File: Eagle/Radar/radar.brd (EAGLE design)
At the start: 100 x 80 mm, 72 parts, among them IC4 MAX414ESD, X1 STEREOJACK, X2 BU-SMA-G, X3 BU-SMA-G, X4 BU-SMA-G

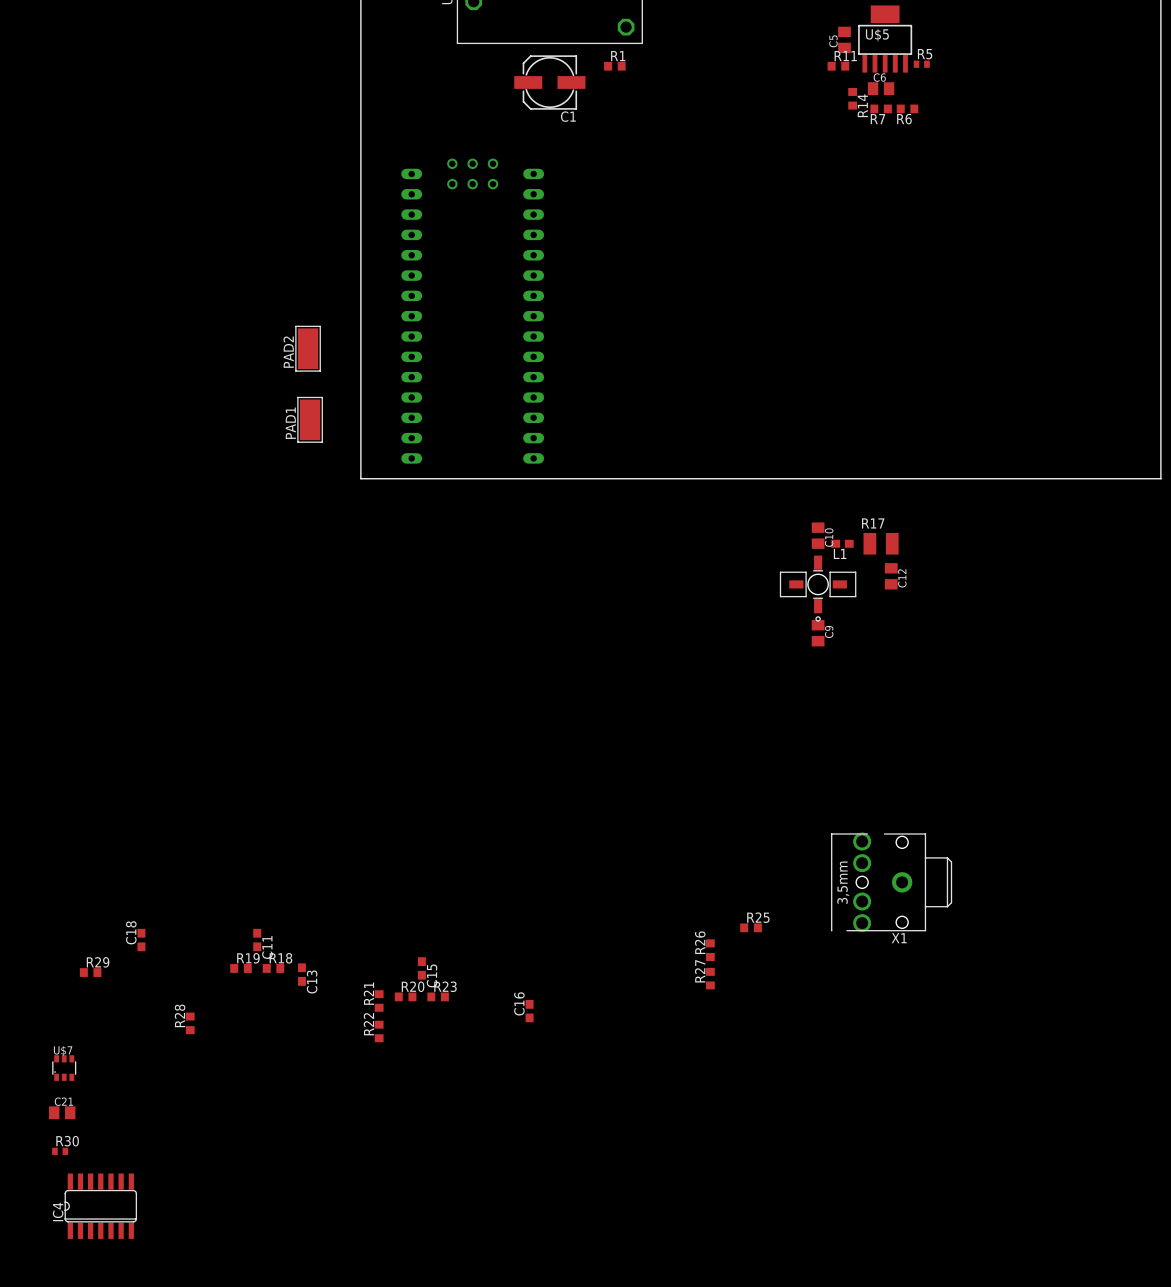
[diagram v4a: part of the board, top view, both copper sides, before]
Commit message: Moved some board parts
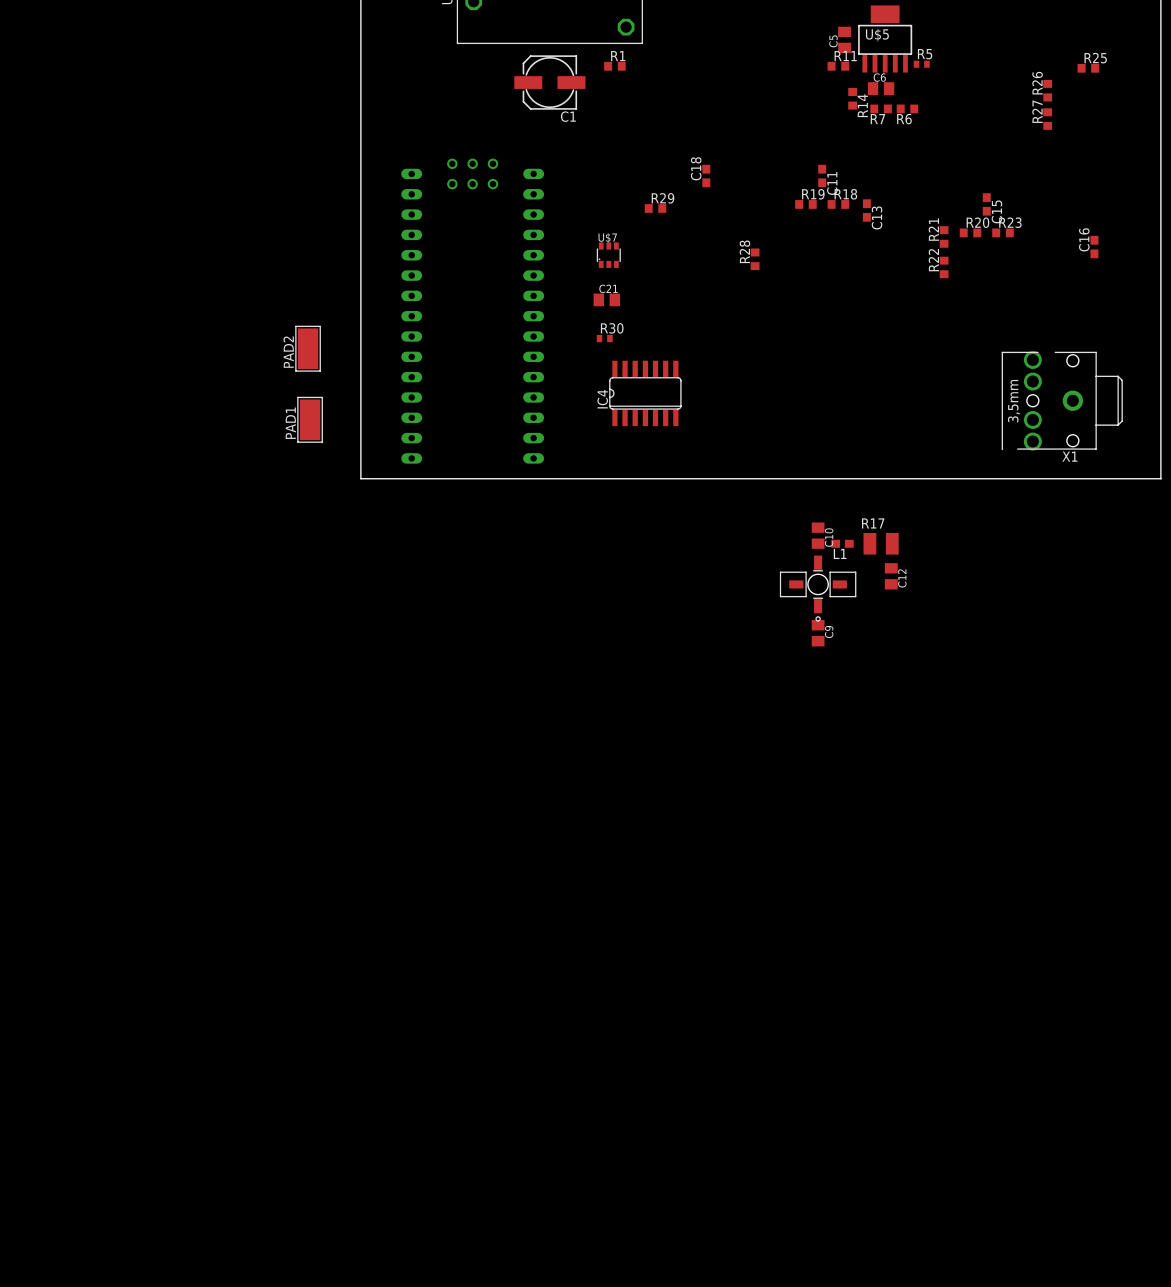
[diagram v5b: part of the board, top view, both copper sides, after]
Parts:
- moved C21 122.3 mm to (30.7, 22.4)
- moved IC4 122.3 mm to (35.6, 10.7)
- moved R30 122.3 mm to (30.5, 17.5)
- moved U$7 122.3 mm to (31.0, 27.9)
- moved C16 118.8 mm to (91.7, 29.0)
- moved R20 118.8 mm to (76.2, 30.7)
- moved R21 118.8 mm to (72.9, 30.2)
- moved R28 118.8 mm to (49.3, 27.4)
- moved C11 118.8 mm to (57.7, 37.8)
- moved C13 118.8 mm to (63.2, 33.5)
- moved C15 118.8 mm to (78.2, 34.3)
- moved C18 118.8 mm to (43.2, 37.8)
- moved R18 118.8 mm to (59.7, 34.3)
- moved R19 118.8 mm to (55.6, 34.3)
- moved R22 118.8 mm to (72.9, 26.4)
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
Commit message: Nearly completed placements on board
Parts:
- removed R11, R12, R13, R14, R25: 0, rcl:R0603
- removed R30, R5: 0, rcl:R0402
- added C24, C25, C8: 10uF, rcl:C0805K
- added L4: 56 nH, radar:0603
- added SJ1, SJ2, SJ3, SJ4, SJ5, SJ6, SJ7, SJ8, SJ9: (no value), jumper:SJ
- added U$11: ERA3+, radar:ERA3+
- R2: value 0 -> 191, 1/2W; device rcl:R0402 -> rcl:R1210
- moved JP3 329.0 mm to (38.4, 74.7)
- moved JP2 321.2 mm to (26.7, 75.7)
- moved JP1 272.4 mm to (32.8, 67.3), turned to 270 degrees
- moved C7 272.3 mm to (82.8, 11.9)
- moved U$10 262.9 mm to (32.8, 62.0)
- moved R32 258.3 mm to (81.8, 18.5)
- moved U$9 256.1 mm to (7.87, 17.0)
- moved R24 255.0 mm to (67.3, 26.7), turned to 270 degrees
- moved L3 252.0 mm to (46.2, 11.2), turned to 270 degrees
- moved U$6 251.0 mm to (39.6, 16.5)
- moved C20 247.9 mm to (81.8, 2.03)
- moved R8 246.1 mm to (73.7, 4.32), turned to 90 degrees
- moved C22 220.1 mm to (60.7, 14.7), turned to 270 degrees
- moved C23 219.1 mm to (50.5, 13.5), turned to 90 degrees
- moved L2 217.4 mm to (27.4, 6.60), turned to 270 degrees
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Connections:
- net N$2 renamed ATTEN_OUT
- net PLL_OUT renamed PLL_IN
- new net LNA_IN: C8.1, U$11.1
- new net LNA_OUT: C24.2, L4.2, U$11.3
- new net LNA_VCC: L4.1, R2.1
- new net MOTOR_GATE: SJ9.2, U$10.1
- new net N$3: C8.2, X3.1
- net AUD1_AC: now also SJ2.2; no longer R25.2
- net GND: now also C25.2, U$11.2, U$11.4
- net LDO1_EN: now also SJ5.2; no longer R2.2
- net LDO1_IN: now also SJ5.1, SJ6.2; no longer R12.2, R2.1
- net LDO1_OUT: now also SJ4.1; no longer R13.1
- net LDO2_EN: now also SJ8.2; no longer R5.2
- net LDO2_IN: now also SJ7.2, SJ8.1; no longer R11.2, R5.1
- net LDO2_OUT: now also SJ3.1; no longer R14.1
- net LFA2_+: now also IC4.12; no longer IC4.5
- net LFA2_-: now also IC4.13; no longer IC4.6
- net LFA2_OUT: now also IC4.14; no longer IC4.7
- net LFA3_OUT: now also SJ2.1; no longer R25.1
- net MAX268X_SHDN: now also SJ1.1; no longer R30.1
- net MOTOR_CTRL: now also SJ9.1; no longer U$10.1
- net PP10V: now also C25.1, R2.2, SJ4.2, SJ7.1; no longer R11.1, R13.2
- net PP10V4: now also SJ6.1; no longer R12.1
- net PP5V: now also SJ1.2, SJ3.2; no longer R14.2, R30.2
- net RF_RX: now also C24.1; no longer X3.1
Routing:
- net LFA1_OUT: track 0.00 -> 2.67 mm
- net LFA2_+: track 0.00 -> 1.86 mm

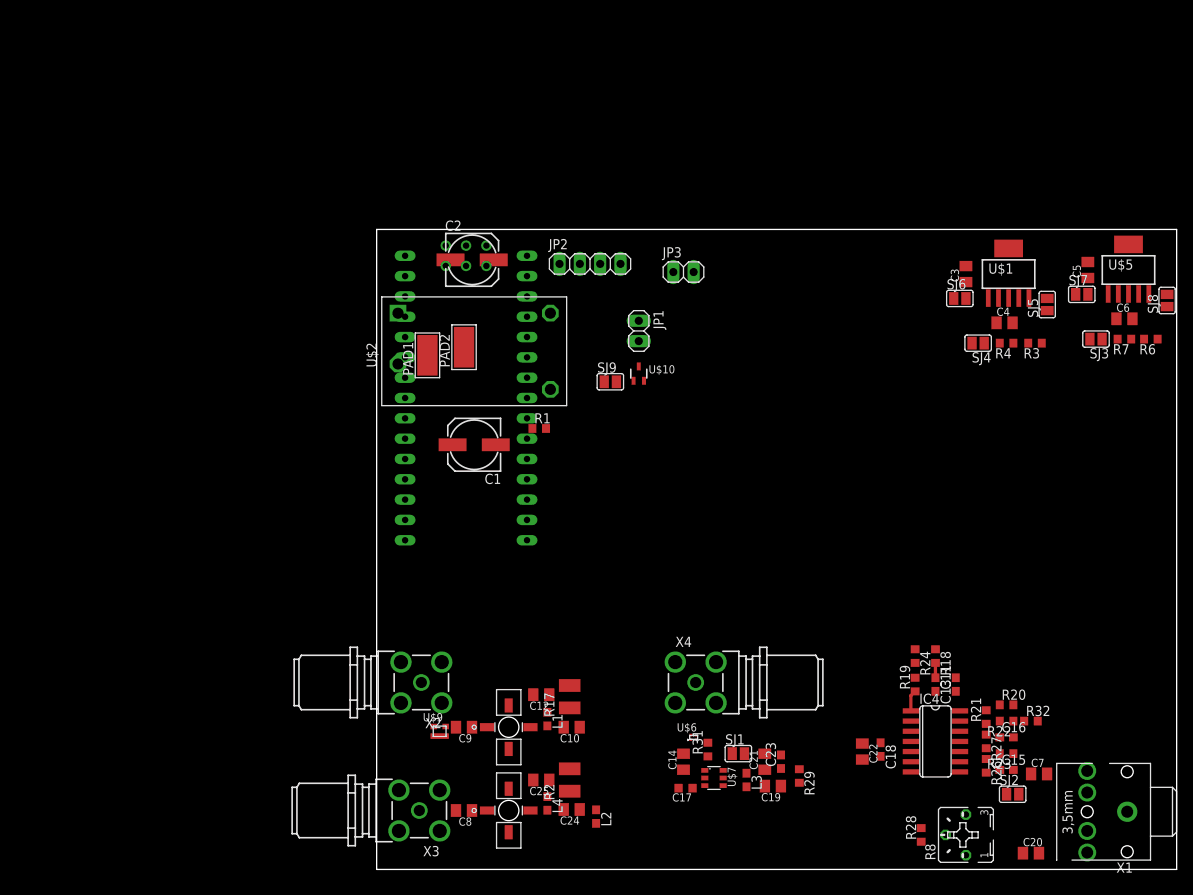
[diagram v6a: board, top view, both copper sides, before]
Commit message: Finished RF routing
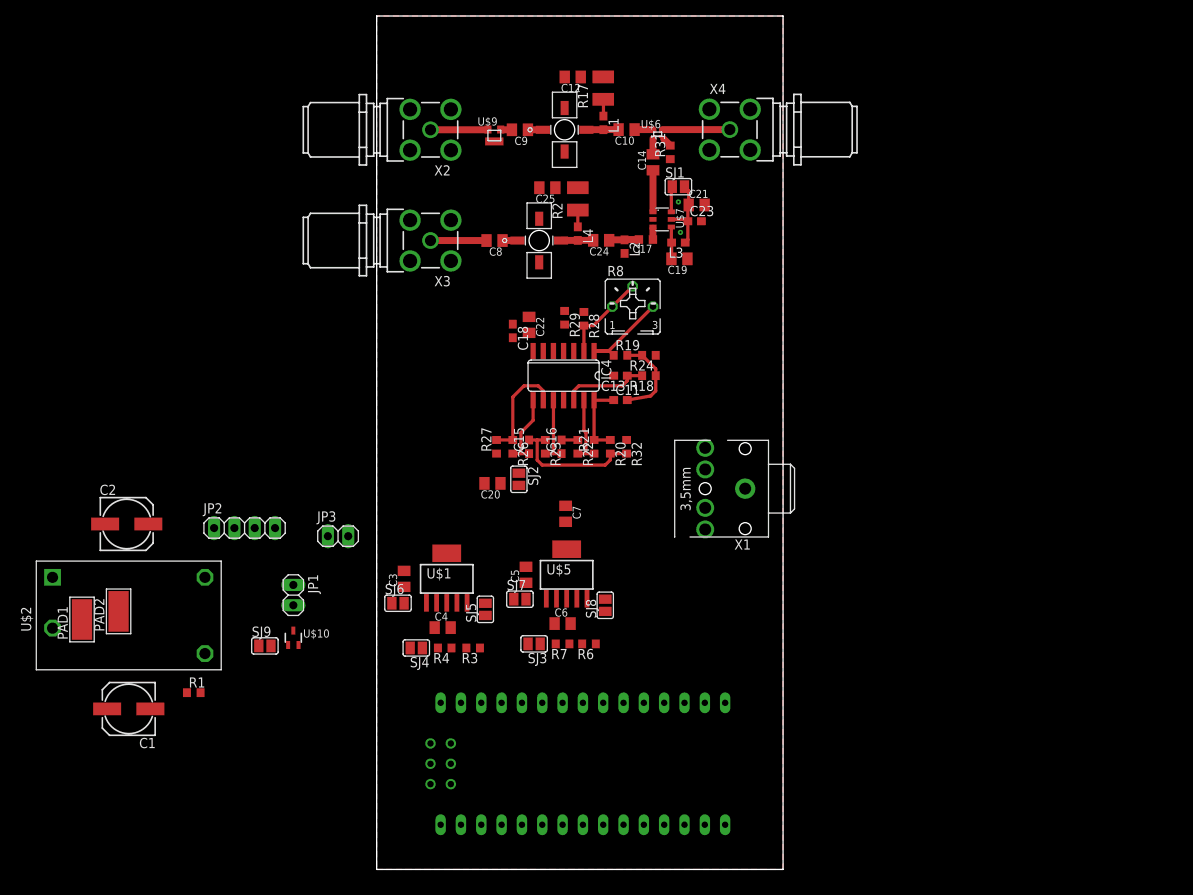
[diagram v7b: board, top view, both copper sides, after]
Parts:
- moved C20 81.7 mm to (14.5, 48.3), turned to 180 degrees
- moved C5 79.9 mm to (18.7, 36.8)
- moved SJ7 79.9 mm to (17.9, 33.8)
- moved U$5 79.9 mm to (23.7, 36.8)
- moved C4 79.9 mm to (8.26, 30.2)
- moved C6 79.9 mm to (23.2, 30.7)
- moved R3 79.9 mm to (12.1, 27.7)
- moved R4 79.9 mm to (8.51, 27.7)
- moved SJ4 79.9 mm to (4.95, 27.7)
- moved SJ8 79.9 mm to (28.6, 33.0)
- moved C3 79.9 mm to (3.43, 36.3)
- moved R6 79.9 mm to (26.5, 28.2)
- moved R7 79.9 mm to (23.2, 28.2)
- moved SJ3 79.9 mm to (19.7, 28.2)
- moved SJ5 79.9 mm to (13.6, 32.5)
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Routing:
- net LFA3_IN: track 0.00 -> 17.0 mm
- net LFA3_-: track 0.00 -> 13.2 mm
- net PP5V: track 0.00 -> 11.5 mm
- net LFA1_-: track 0.00 -> 11.3 mm
- net LFA2_IN: track 0.00 -> 10.9 mm
- net LFA3_OUT: track 0.00 -> 9.71 mm
- net LFA1_OUT: track 2.67 -> 12.3 mm
- net LFA2_OUT: track 0.00 -> 9.45 mm
- net LFA2_-: track 0.00 -> 9.18 mm
- net LFA3_+: track 0.00 -> 9.08 mm
- net LFA2_+: track 1.86 -> 10.9 mm
- net COUPLER_OUT: track 0.00 -> 8.79 mm
- net PLL_IN: track 0.00 -> 7.33 mm
- net N$3: track 0.00 -> 7.00 mm
- net MIXER_LO: track 0.00 -> 5.19 mm
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- added copper zone on layer 1, net GND
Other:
- board size 100 x 80 mm -> 50.8 x 106.7 mm

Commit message: Routing complete
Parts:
- removed SJ5, SJ8: (no value), jumper:SJ
- added C26, C27, C28: 0.1u, rcl:C0603
- added JP4: (no value), pinhead:1X02
- moved PAD1 110.8 mm to (46.6, 104.1), turned to 90 degrees
- moved PAD2 92.8 mm to (26.8, 103.9), turned to 90 degrees
- moved JP2 65.4 mm to (48.4, 34.4), turned to 270 degrees
- moved C1 59.8 mm to (19.2, 52.7), turned to 0 degrees
- moved JP1 59.7 mm to (48.4, 24.3), turned to 90 degrees
- moved JP3 58.8 mm to (48.4, 16.6), turned to 270 degrees
- moved SJ9 50.3 mm to (35.8, 21.0)
- moved U$10 47.8 mm to (37.2, 24.6)
- moved U$2 44.2 mm to (12.1, 41.8), turned to 180 degrees
- moved R3 43.6 mm to (2.67, 70.2), turned to 0 degrees
- moved SJ4 43.0 mm to (9.40, 70.5), turned to 0 degrees
- moved R4 42.6 mm to (5.71, 70.2), turned to 0 degrees
- moved C2 41.6 mm to (9.27, 52.7), turned to 180 degrees
- moved R1 38.6 mm to (2.54, 51.2), turned to 270 degrees
- moved C4 37.5 mm to (6.48, 67.7), turned to 180 degrees
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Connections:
- removed net LDO1_EN: SJ5.2, U$1.5
- removed net LDO2_EN: SJ8.2, U$5.5
- net ENCODER_A: now also U$3.D2
- net ENCODER_B: now also U$3.D3; no longer U$3.D2
- net GND: now also C26.2, C27.2, C28.2, JP4.2
- net LDO1_IN: now also U$1.5; no longer SJ5.1
- net LDO2_IN: now also U$5.5; no longer SJ8.1
- net PP10V: now also JP4.1
- net PP5V: now also C26.1, C27.1, C28.1
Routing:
- net PP5V: track 11.5 -> 148.0 mm, vias 0 -> 6
- net PP10V: track 0.00 -> 128.2 mm
- net PPUSB: track 0.00 -> 71.1 mm, vias 0 -> 1
- net ENCODER_A: track 0.00 -> 49.9 mm
- net ENCODER_B: track 0.00 -> 45.3 mm
- net PP10V4: track 0.00 -> 27.2 mm
- net AUD1_AC: track 0.00 -> 18.7 mm
- net MOTOR_CTRL: track 0.00 -> 15.6 mm
- net LDO1_IN: track 0.00 -> 15.2 mm, vias 0 -> 2
- net LDO2_IN: track 0.00 -> 15.1 mm, vias 0 -> 2
- net N$1: track 0.00 -> 11.2 mm
- net LDO2_OUT: track 0.00 -> 9.94 mm
- net LDO1_OUT: track 0.00 -> 8.17 mm
- net LDO2_FB: track 0.00 -> 7.29 mm
- net LDO1_FB: track 0.00 -> 7.26 mm
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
